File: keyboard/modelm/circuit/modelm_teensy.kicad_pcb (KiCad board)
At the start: 2 copper layers, 146 x 50.8 mm, 9 parts, among them SW1 SW_PUSH, U1 TEENSYPP2

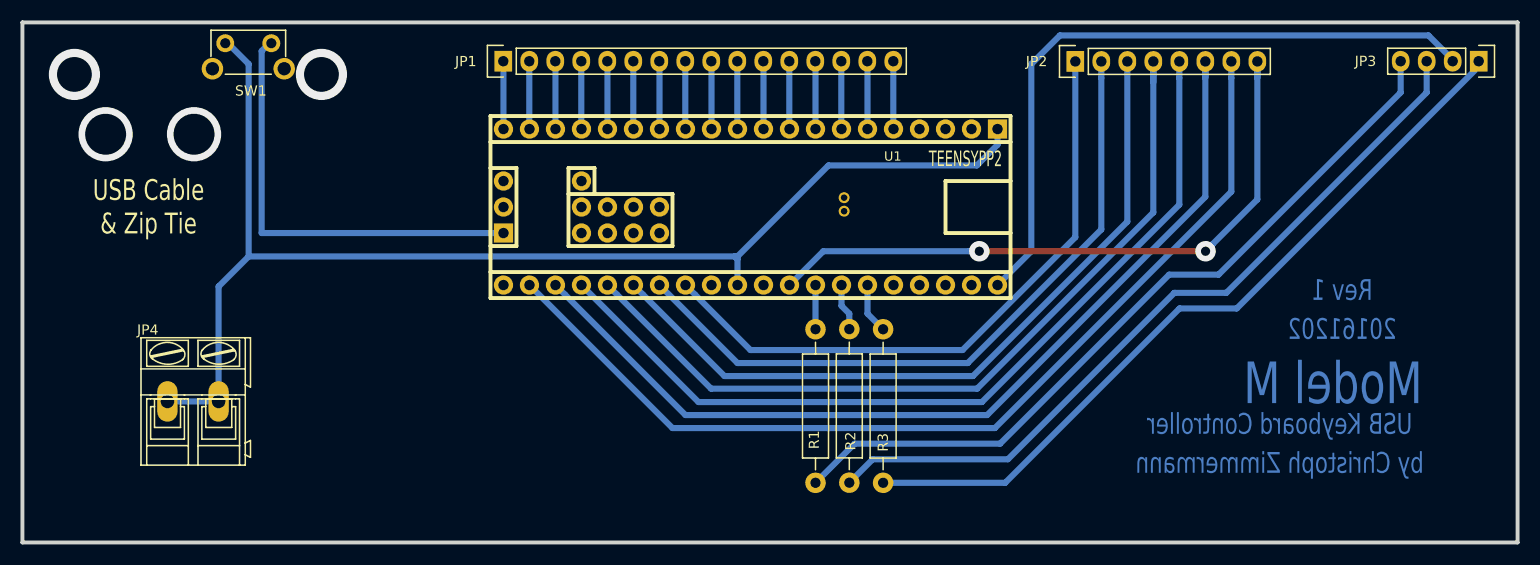
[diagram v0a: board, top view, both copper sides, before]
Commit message: Corrected LED connector orientation
The connector for the LEDs was wrongly rotated by 180°. This is fixed now.
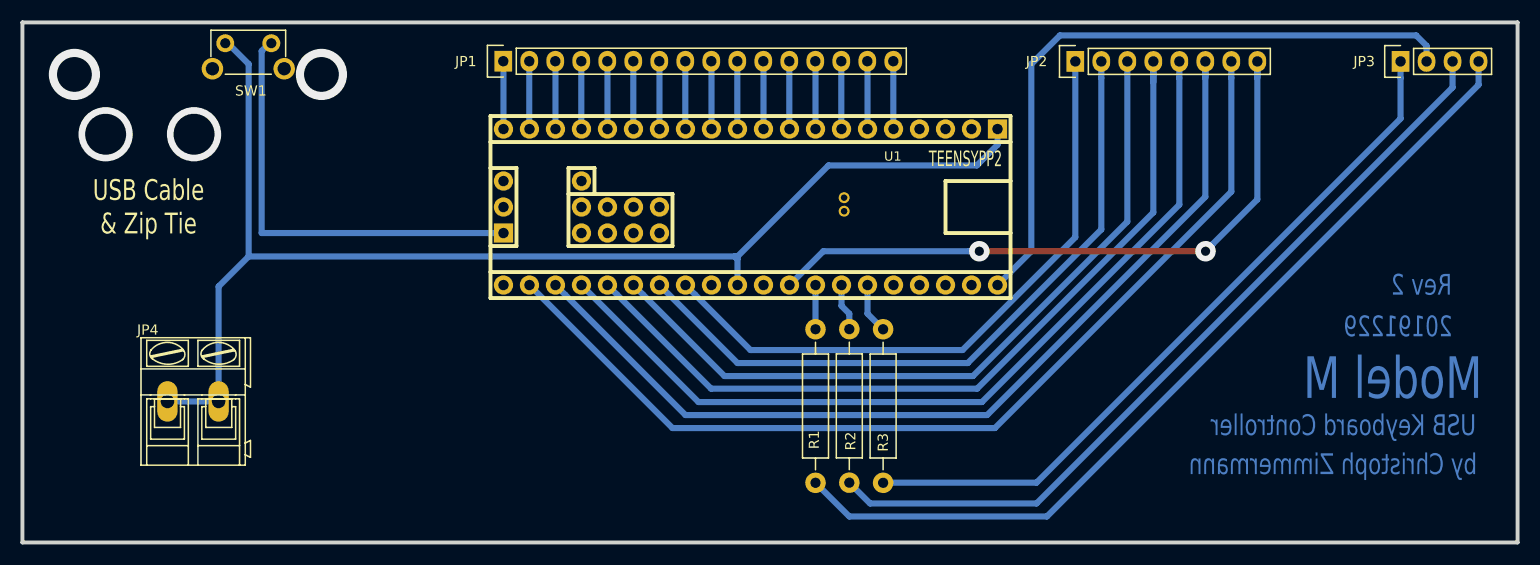
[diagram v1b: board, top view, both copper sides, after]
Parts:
- JP4: value CONN_01X02 -> 6.3 mm
- SW1: value SW_PUSH -> Reset
- moved JP3 7.63 mm to (191.8, 58.4), turned to 90 degrees
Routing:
- net Net-(JP3-Pad4): track 76.0 -> 85.9 mm
- net Net-(JP3-Pad1): track 75.5 -> 70.9 mm
- net Net-(JP3-Pad3): track 75.4 -> 79.1 mm
- net VCC: track 66.6 -> 64.7 mm
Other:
- board text added: "20191229"
- board text added: "Rev 2"
- board text removed: "20161202"
- board text removed: "Rev 1"
